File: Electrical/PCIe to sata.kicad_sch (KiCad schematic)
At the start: 64 parts, among them J10 87427-0442, J13 SATA-A-PL-SMT-K, J14 SATA-A-PL-SMT-K, J19 SATA-A-PL-SMT-K, J20 SATA-A-PL-SMT-K, J21 SATA-A-PL-SMT-K, J22 SATA-A-PL-SMT-K, J7 87427-0442, J8 87427-0442, J9 87427-0442, U11 W25Q128JVSIQ, U8 ASM1166, Y2 25MHz

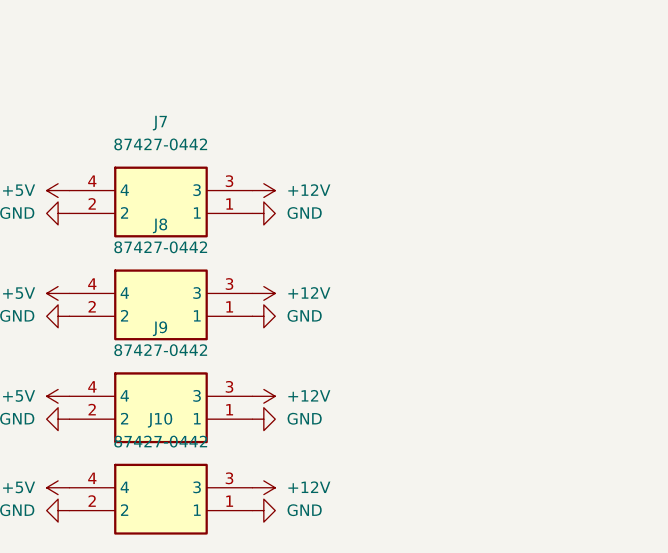
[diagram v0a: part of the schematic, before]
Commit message: replace the 12v buck with a 12 amp capable buck
also removed soft start circuit because its built in the Buck Converter IC
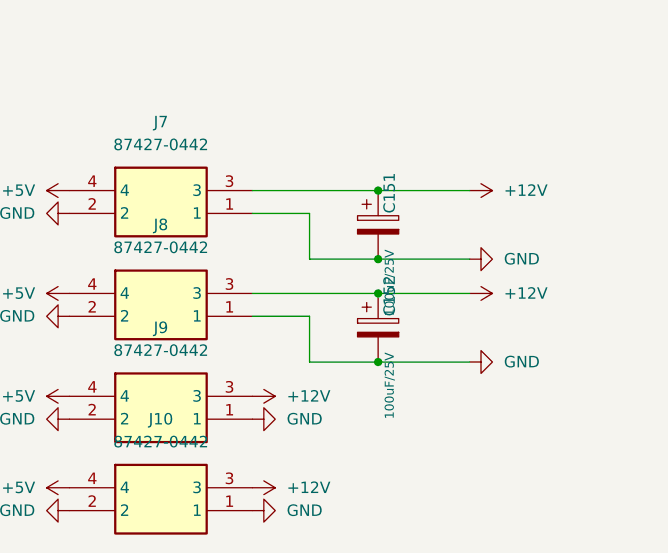
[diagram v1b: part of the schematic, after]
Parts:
- added C151, C152: 100uF/25V, A_HDJ_Library:CP_Elec_6.3x7.7, symbol Device:C_Polarized
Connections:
- net +12V: now also C151.1, C152.1
- net GND: now also C151.2, C152.2

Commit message: Add step down converter
Prevent 20v going into the lattepanda mu, it has been stepped down to 15v
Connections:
- net +5V: now also J10.2, J7.2, J8.2, J9.2; no longer J10.4, J7.4, J8.4, J9.4
- net GND: now also J10.4, J7.4, J8.4, J9.4; no longer J10.2, J7.2, J8.2, J9.2

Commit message: Major Overhaul
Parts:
- removed C10, C9: C, Capacitor_SMD:C_0402_1005Metric, symbol 100nf cap:C
- removed C101, C102, C103: 10uF/10V, Capacitor_SMD:C_0402_1005Metric, symbol Device:C
- removed D19: D_Schottky, Diode_SMD:D_SOD-923, symbol Device:D_Schottky
- removed R91: ERA-3AED162V, ERA3AEB101V, symbol 1.6k resis:ERA-3AED162V
- added C10, C101, C102, C103, C166, C167, C168, C169, C170, C171, C172, C173, C174, C175, C176, C177, C178, C179, C180, C181, C182, C183, C184, C9: 10nF/50V, A_HDJ_Library:C_0402_1005Metric, symbol Device:C_Small
- added C116, C117, C118, C119, C185, C186, C187, C188: 100nF/50V, Capacitor_SMD:C_0402_1005Metric, symbol 100nf cap:C
- added C155: 100nF/50V, Capacitor_SMD:C_0402_1005Metric, symbol Device:C
- added C157, C158, C159, C160, C161, C162, C163, C164: 220nF/50V, A_HDJ_Library:C_0402_1005Metric, symbol Device:C_Small
- added C165: 4.7uF/50V, Capacitor_SMD:C_0402_1005Metric, symbol 100nf cap:C
- added C189, C190: 100uF/25V, A_HDJ_Library:CP_Elec_6.3x7.7, symbol Device:C_Polarized
- added R190: 0R/1%, A_HDJ_Library:R_0402_1005Metric, symbol Device:R
- added R24: 12K/1%, Resistor_SMD:R_0402_1005Metric, symbol Device:R
- C100, C104, C94, C95, C96, C97, C98, C99: value 10uF/10V -> 100nF/50V
- C105, C106, C107, C108, C109, C11, C7, C8, C92, C93: value C -> 100nF/50V
- C151, C152: value 100uF/25V -> 220uF/50V
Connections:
- net +12V: now also C116.1, C117.1, C118.1, C119.2
- net +1V0: now also C98.1; no longer C98.2
- net +2V5: now also C93.1; no longer C93.2, U8.57 (VCC25O)
- net +3V3: now also U11.3 (IO2), U11.7 (IO3), U11.8 (VCC), C155.1; no longer R78.2, R79.2, R87.2, R88.2, R89.2, R90.2
- net +5V: now also C185.2, C186.2, C187.2, C188.2, C189.2, C190.2
- net GND: now also C93.2, C98.2, R78.2, R79.2, R87.2, R88.2, R89.2, R90.2, C116.2, C117.2, C118.2, C119.1, C155.2, C165.1, C185.1, C186.1, C187.1, C188.1, C189.1, C190.1, R24.2; no longer C93.1, C98.1, C99.1
- net PCIE_RX_3+: now also C159.1; no longer U8.48 (PETXP0)
- net PCIE_RX_3-: now also C158.1; no longer U8.49 (PETXN0)
- net PCIE_RX_4+: now also C160.1; no longer U8.51 (PETXP1)
- net PCIE_RX_4-: now also C157.1; no longer U8.52 (PETXN1)
- net PCIE_TX_3+: now also C162.1; no longer U8.45 (PERXP0)
- net PCIE_TX_3-: now also C164.1; no longer U8.46 (PERXN0)
- net PCIE_TX_4+: now also C161.1; no longer U8.54 (PERXP1)
- net PCIE_TX_4-: now also C163.1; no longer U8.55 (PERXN1)
- net RX_N_0: now also C10.2; no longer J21.S5 (B-)
- net RX_N_1: now also C167.2; no longer J22.S5 (B-)
- net RX_N_2: now also C178.2; no longer J19.S5 (B-)
- net RX_N_3: now also C182.2; no longer J20.S5 (B-)
- net RX_N_4: now also C171.2; no longer J14.S5 (B-)
- net RX_N_5: now also C175.2; no longer J13.S5 (B-)
- net RX_P_0: now also C9.2; no longer J21.S6 (B+)
- net RX_P_1: now also C168.2; no longer J22.S6 (B+)
- net RX_P_2: now also C177.2; no longer J19.S6 (B+)
- net RX_P_3: now also C181.2; no longer J20.S6 (B+)
- net RX_P_4: now also C172.2; no longer J14.S6 (B+)
- net RX_P_5: now also C176.2; no longer J13.S6 (B+)
- net TX_N_0: now also C101.2; no longer J21.S3 (A-)
- net TX_N_1: now also C166.2; no longer J22.S3 (A-)
- net TX_N_2: now also C179.2; no longer J19.S3 (A-)
- net TX_N_3: now also C183.2; no longer J20.S3 (A-)
- net TX_N_4: now also C170.2; no longer J14.S3 (A-)
- net TX_N_5: now also C174.2; no longer J13.S3 (A-)
- net TX_P_0: now also C102.2; no longer J21.S2 (A+)
- net TX_P_1: now also C103.2; no longer J22.S2 (A+)
- net TX_P_2: now also C180.2; no longer J19.S2 (A+)
- net TX_P_3: now also C184.2; no longer J20.S2 (A+)
- net TX_P_4: now also C169.2; no longer J14.S2 (A+)
- net TX_P_5: now also C173.2; no longer J13.S2 (A+)
- net at U8.67 (REXT): now also R24.1
- net at U11.2 (DO(IO1)), U8.87 (SPI_DIO): now also R190.1; no longer U11.5 (DI(IO0))
- new net: C102.1, J21.S2 (A+)
- new net: C101.1, J21.S3 (A-)
- new net: C10.1, J21.S5 (B-)
- new net: C9.1, J21.S6 (B+)
- new net: R190.2, U11.5 (DI(IO0))
- new net: C162.2, U8.45 (PERXP0)
- new net: C164.2, U8.46 (PERXN0)
- new net: C159.2, U8.48 (PETXP0)
- new net: C158.2, U8.49 (PETXN0)
- new net: C160.2, U8.51 (PETXP1)
- new net: C157.2, U8.52 (PETXN1)
- new net: C161.2, U8.54 (PERXP1)
- new net: C163.2, U8.55 (PERXN1)
- new net: C103.1, J22.S2 (A+)
- new net: C170.1, J14.S3 (A-)
- new net: C184.1, J20.S2 (A+)
- new net: C183.1, J20.S3 (A-)
- new net: C182.1, J20.S5 (B-)
- new net: C181.1, J20.S6 (B+)
- new net: C169.1, J14.S2 (A+)
- new net: C166.1, J22.S3 (A-)
- new net: C167.1, J22.S5 (B-)
- new net: C168.1, J22.S6 (B+)
- new net: C173.1, J13.S2 (A+)
- new net: C174.1, J13.S3 (A-)
- new net: C175.1, J13.S5 (B-)
- new net: C176.1, J13.S6 (B+)
- new net: C177.1, J19.S6 (B+)
- new net: C178.1, J19.S5 (B-)
- new net: C171.1, J14.S5 (B-)
- new net: C180.1, J19.S2 (A+)
- new net: C179.1, J19.S3 (A-)
- new net: C172.1, J14.S6 (B+)
- new net VCC25O: C165.2, U8.57 (VCC25O)
- no-connect marks 9 -> 7
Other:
- moved on the sheet: C100, C104, C105, C106, C107, C108, C109, C11, C7, C8, C92, C93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

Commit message: Update Board According to DFA Review
Updated Ethernet Jack
Updated L3 Inductor
Fixed a few errors
Updated mounting hole size
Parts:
- added C191: 100nF/50V, Capacitor_SMD:C_0402_1005Metric, symbol Device:C
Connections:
- net +1V0: now also C191.1
- net GND: now also C191.2
